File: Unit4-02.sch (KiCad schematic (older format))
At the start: 5 parts

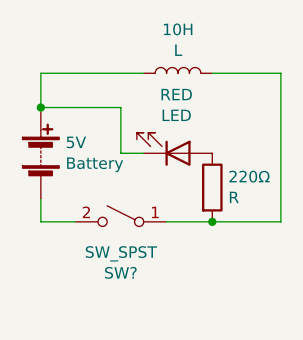
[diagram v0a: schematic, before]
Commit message: Modified switch type
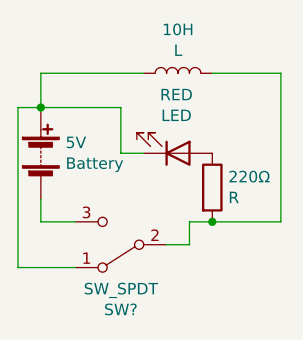
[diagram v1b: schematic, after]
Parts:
- removed SW?: SW_SPST, symbol Switch:SW_SPST
- added SW?: SW_SPDT, symbol Switch:SW_SPDT
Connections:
- net at 10H.1, 5V.1 (+), RED.1 (K): now also SW?.1 (A)
- net at 5V.2 (-): now also SW?.3 (C)
- net at 10H.2, 220Ω.2: now also SW?.2 (B)
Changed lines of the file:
@@
 	1    0    0    1
-$EndComp
-$Comp
-L Switch:SW_SPST SW?
-U 1 1 65090D76
-P 3400 3450
-F 0 "SW?" H 3400 3225 50  0000 C CNN
-F 1 "SW_SPST" H 3400 3316 50  0000 C CNN
-F 2 "" H 3400 3450 50  0001 C CNN
-F 3 "~" H 3400 3450 50  0001 C CNN
-	1    3400 3450
-	-1   0    0    -1
 $EndComp
 Wire Wire Line
@@
 Wire Wire Line
 	3050 2950 3050 2800
-Wire Wire Line
-	3600 3450 3800 3450
 Connection ~ 3050 2950
 $Comp
@@
 Wire Wire Line
 	4100 2800 4100 3450
-Connection ~ 3800 3450
 Wire Wire Line
 	3800 2800 4100 2800
 Wire Wire Line
 	3800 3450 4100 3450
+$Comp
+L Switch:SW_SPDT SW?
+U 1 1 6509EB2B
+P 3400 3550
+F 0 "SW?" H 3400 3835 50  0000 C CNN
+F 1 "SW_SPDT" H 3400 3744 50  0000 C CNN
+F 2 "" H 3400 3550 50  0001 C CNN
+F 3 "~" H 3400 3550 50  0001 C CNN
+	1    3400 3550
+	-1   0    0    1
+$EndComp
+Wire Wire Line
+	3800 3450 3700 3450
+Wire Wire Line
+	3700 3550 3700 3450
+Wire Wire Line
+	3700 3550 3600 3550
+Connection ~ 3800 3450
+Wire Wire Line
+	3200 3650 2950 3650
+Wire Wire Line
+	2950 3650 2950 2950
+Wire Wire Line
+	2950 2950 3050 2950
 $EndSCHEMATC
